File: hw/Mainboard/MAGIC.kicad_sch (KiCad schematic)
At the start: 18 parts, among them U7 SN74LVC4245APWR, U8 SN74LVC4245APWR, U9 SN74LVC4245APWR

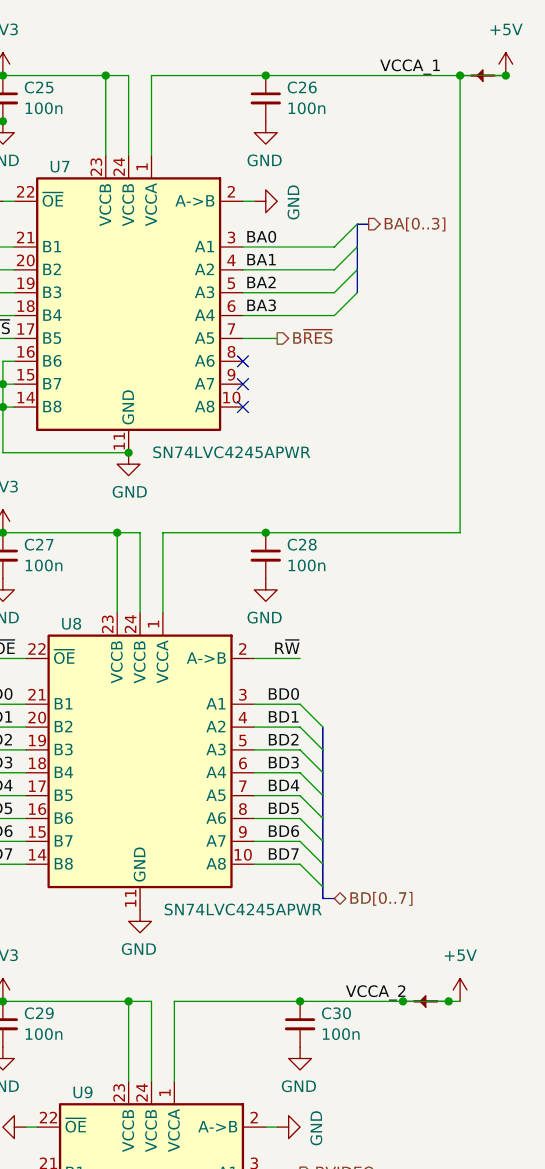
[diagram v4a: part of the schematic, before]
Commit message: hw: remove net/power ties
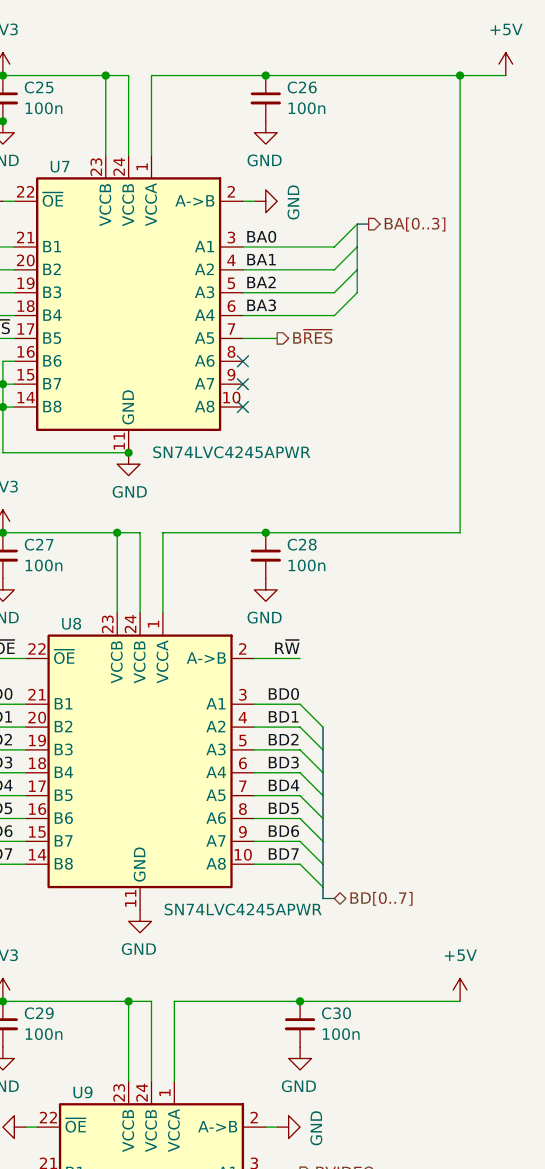
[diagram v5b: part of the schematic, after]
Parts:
- removed PT13, PT14: PowerTie_2, PET:NetTie-2_SMD_Pad_1.6_to_0.4mm, symbol PET:PowerTie_2
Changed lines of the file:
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@@
   (junction (at 207.01 57.15) (diameter 0) (color 0 0 0 0)
   )
-  (junction (at 262.89 20.32) (diameter 0) (color 0 0 0 0)
-  )
   (junction (at 220.98 62.23) (diameter 0) (color 0 0 0 0)
   )
   (junction (at 92.71 124.46) (diameter 0) (color 0 0 0 0)
   )
-  (junction (at 251.46 123.19) (diameter 0) (color 0 0 0 0)
-  )
   (junction (at 207.01 71.12) (diameter 0) (color 0 0 0 0)
   )
@@
   )
   (junction (at 96.52 116.84) (diameter 0) (color 0 0 0 0)
-  )
-  (junction (at 256.54 123.19) (diameter 0) (color 0 0 0 0)
   )
   (junction (at 219.71 71.12) (diameter 0) (color 0 0 0 0)
@@
     (stroke (width 0) (type default) (color 0 0 0 0))
   )
-  (wire (pts (xy 240.03 123.19) (xy 251.46 123.19))
+  (wire (pts (xy 240.03 123.19) (xy 257.81 123.19))
     (stroke (width 0) (type default) (color 0 0 0 0))
   )
@@
     (stroke (width 0) (type default) (color 0 0 0 0))
   )
-  (wire (pts (xy 251.46 123.19) (xy 256.54 123.19))
-    (stroke (width 0) (type default) (color 0 0 0 0))
-  )
   (wire (pts (xy 240.03 102.87) (xy 234.95 102.87))
     (stroke (width 0) (type default) (color 0 0 0 0))
@@
   )
   (bus (pts (xy 203.2 107.95) (xy 203.2 110.49))
-    (stroke (width 0) (type default) (color 0 0 0 0))
-  )
-  (wire (pts (xy 256.54 123.19) (xy 257.81 123.19))
     (stroke (width 0) (type default) (color 0 0 0 0))
   )
@@
     (effects (font (size 1.27 1.27)) (justify left bottom))
   )
-  (label "VCCA_1" (at 248.92 20.32 0)
-    (effects (font (size 1.27 1.27)) (justify left bottom))
-  )
   (label "A1" (at 201.93 41.91 0)
     (effects (font (size 1.27 1.27)) (justify left bottom))
@@
   )
   (label "D2" (at 205.74 95.25 0)
-    (effects (font (size 1.27 1.27)) (justify left bottom))
-  )
-  (label "VCCA_2" (at 245.11 123.19 0)
     (effects (font (size 1.27 1.27)) (justify left bottom))
   )
@@
     (pin "2")
   )
-  (symbol (lib_id "PET:PowerTie_2") (at 254 123.19 180) (unit 1)
-    (in_bom yes) (on_board yes) (fields_autoplaced)
-    (property "Reference" "PT14" (id 0) (at 254 125.095 0)
-      (effects (font (size 1.27 1.27)) hide)
-    )
-    (property "Value" "PowerTie_2" (id 1) (at 254 121.285 0)
-      (effects (font (size 1.27 1.27)) hide)
-    )
-    (property "Footprint" "PET:NetTie-2_SMD_Pad_1.6_to_0.4mm" (id 2) (at 254 123.19 0)
-      (effects (font (size 1.27 1.27)) hide)
-    )
-    (property "Datasheet" "~" (id 3) (at 254 123.19 0)
-      (effects (font (size 1.27 1.27)) hide)
-    )
-    (pin "1")
-    (pin "2")
-  )
   (symbol (lib_id "power:GND") (at 92.71 125.73 0) (unit 1)
     (in_bom yes) (on_board yes) (fields_autoplaced)
@@
     (pin "1")
   )
-  (symbol (lib_id "PET:PowerTie_2") (at 260.35 20.32 180) (unit 1)
-    (in_bom yes) (on_board yes) (fields_autoplaced)
-    (property "Reference" "PT13" (id 0) (at 260.35 22.225 0)
-      (effects (font (size 1.27 1.27)) hide)
-    )
-    (property "Value" "PowerTie_2" (id 1) (at 260.35 18.415 0)
-      (effects (font (size 1.27 1.27)) hide)
-    )
-    (property "Footprint" "PET:NetTie-2_SMD_Pad_1.6_to_0.4mm" (id 2) (at 260.35 20.32 0)
-      (effects (font (size 1.27 1.27)) hide)
-    )
-    (property "Datasheet" "~" (id 3) (at 260.35 20.32 0)
-      (effects (font (size 1.27 1.27)) hide)
-    )
-    (pin "1")
-    (pin "2")
-  )
   (symbol (lib_id "power:+3V3") (at 207.01 123.19 0) (mirror y) (unit 1)

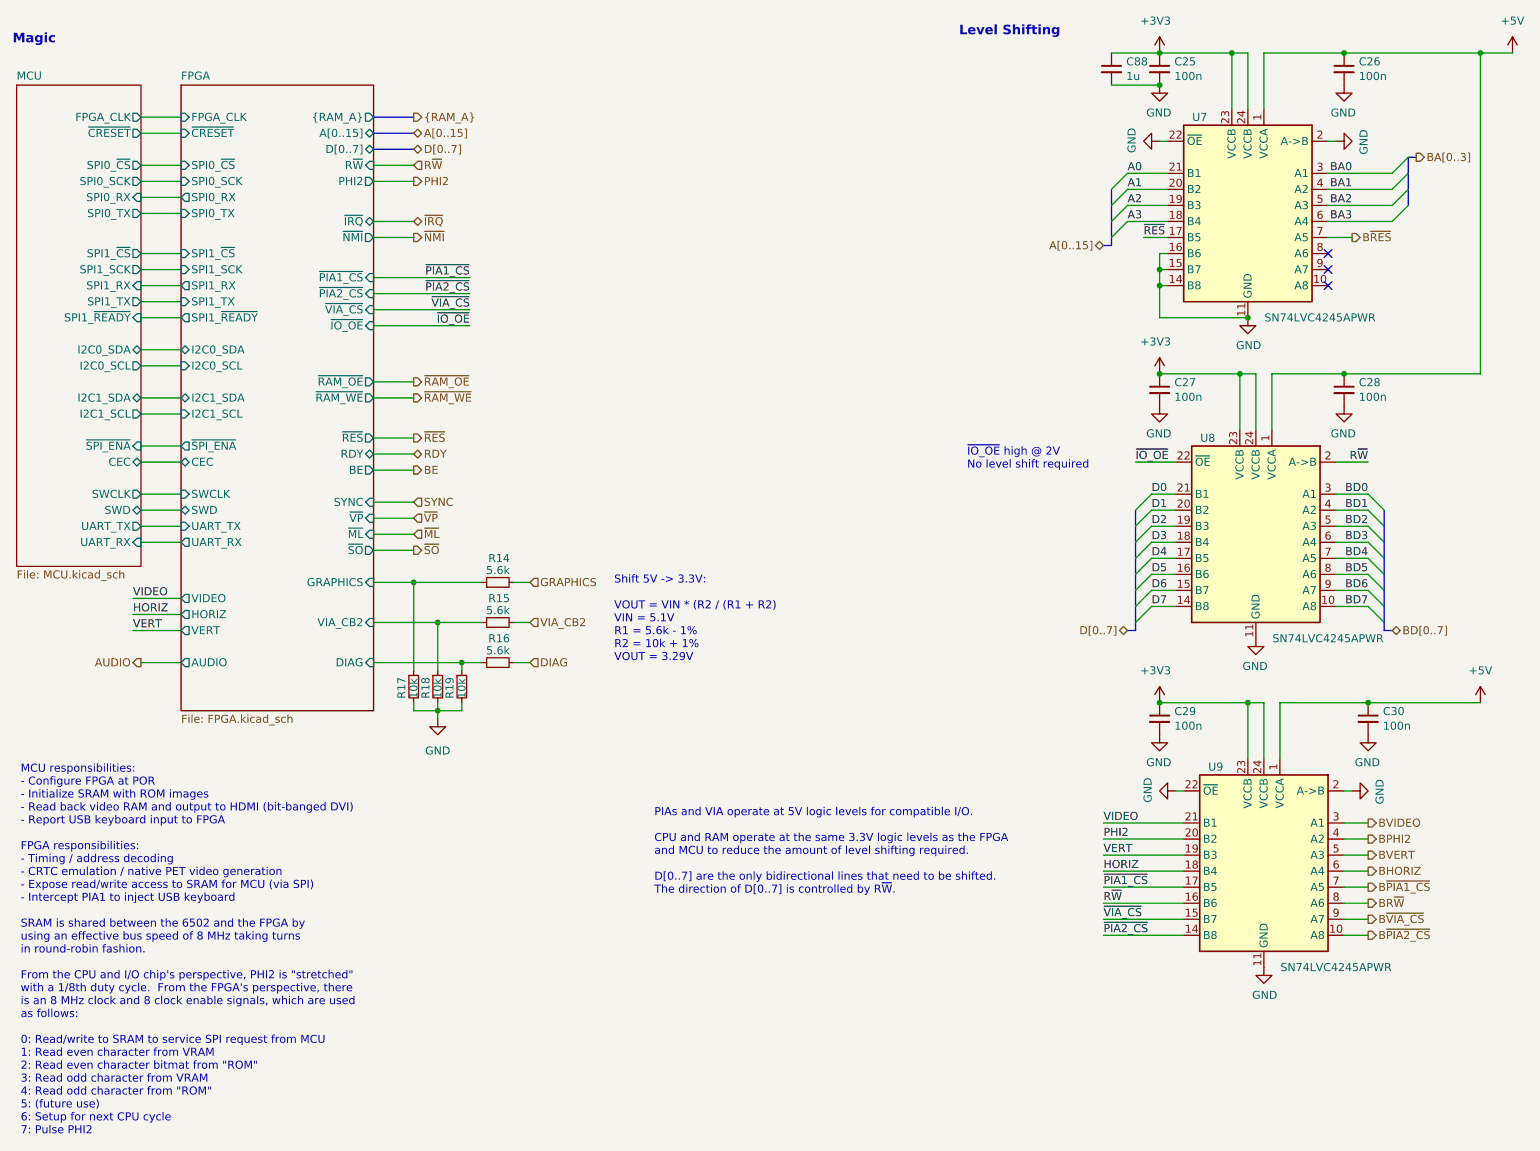
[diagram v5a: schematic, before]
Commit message: hw: renumber J* refs to match PET connectors
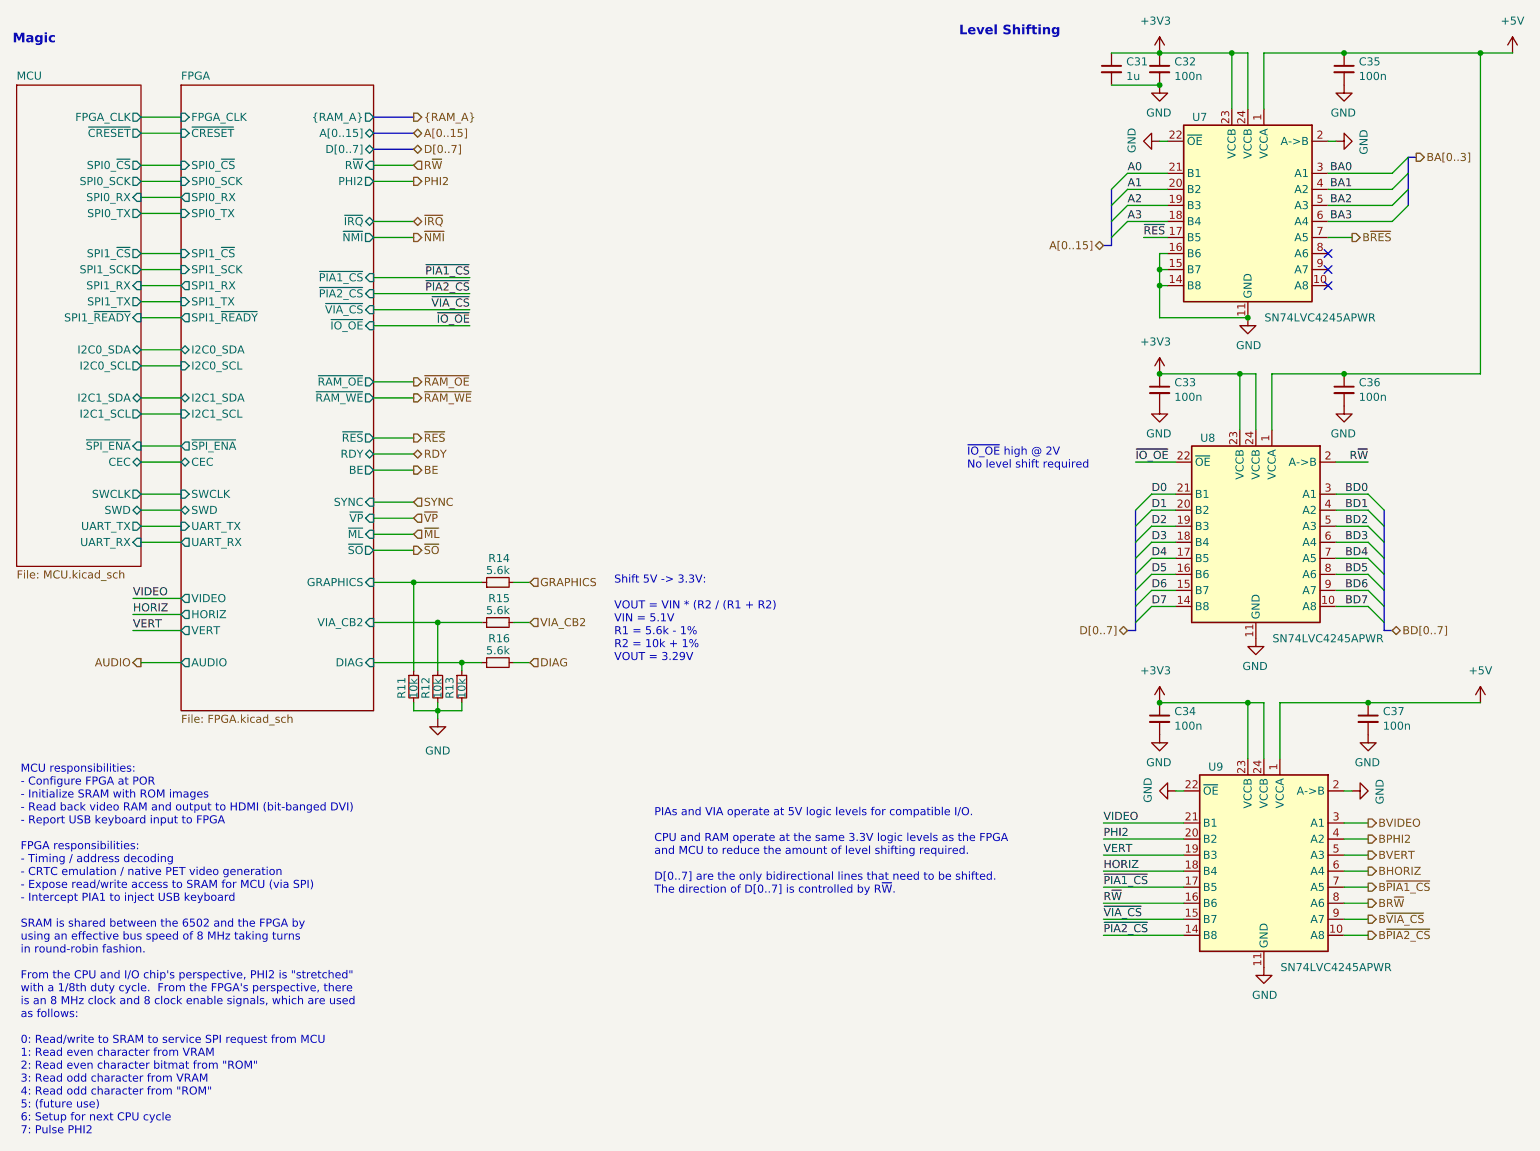
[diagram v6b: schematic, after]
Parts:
- renumbered C88 to C31, C25 to C32, C27 to C33, C29 to C34, C26 to C35, C28 to C36, C30 to C37, R17 to R11, R18 to R12, R19 to R13
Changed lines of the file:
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@@
   (symbol (lib_id "power:+3V3") (at 207.01 71.12 0) (mirror y) (unit 1)
     (in_bom yes) (on_board yes)
-    (property "Reference" "#PWR041" (id 0) (at 207.01 74.93 0)
+    (property "Reference" "#PWR037" (id 0) (at 207.01 74.93 0)
       (effects (font (size 1.27 1.27)) hide)
     )
@@
   (symbol (lib_id "power:GND") (at 220.98 62.23 0) (unit 1)
     (in_bom yes) (on_board yes)
-    (property "Reference" "#PWR040" (id 0) (at 220.98 68.58 0)
+    (property "Reference" "#PWR042" (id 0) (at 220.98 68.58 0)
       (effects (font (size 1.27 1.27)) hide)
     )
@@
   (symbol (lib_id "power:GND") (at 222.25 113.03 0) (mirror y) (unit 1)
     (in_bom yes) (on_board yes)
-    (property "Reference" "#PWR044" (id 0) (at 222.25 119.38 0)
+    (property "Reference" "#PWR043" (id 0) (at 222.25 119.38 0)
       (effects (font (size 1.27 1.27)) hide)
     )
@@
   (symbol (lib_id "power:GND") (at 223.52 165.1 0) (unit 1)
     (in_bom yes) (on_board yes)
-    (property "Reference" "#PWR052" (id 0) (at 223.52 171.45 0)
+    (property "Reference" "#PWR044" (id 0) (at 223.52 171.45 0)
       (effects (font (size 1.27 1.27)) hide)
     )
@@
   (symbol (lib_id "power:GND") (at 207.01 34.29 270) (mirror x) (unit 1)
     (in_bom yes) (on_board yes)
-    (property "Reference" "#PWR038" (id 0) (at 200.66 34.29 0)
+    (property "Reference" "#PWR036" (id 0) (at 200.66 34.29 0)
       (effects (font (size 1.27 1.27)) hide)
     )
@@
   (symbol (lib_id "Device:C_Small") (at 207.01 22.86 0) (unit 1)
     (in_bom yes) (on_board yes)
-    (property "Reference" "C25" (id 0) (at 209.3468 21.6916 0)
+    (property "Reference" "C32" (id 0) (at 209.3468 21.6916 0)
       (effects (font (size 1.27 1.27)) (justify left))
     )
@@
   (symbol (lib_id "Device:C_Small") (at 207.01 125.73 0) (unit 1)
     (in_bom yes) (on_board yes)
-    (property "Reference" "C29" (id 0) (at 209.3468 124.5616 0)
+    (property "Reference" "C34" (id 0) (at 209.3468 124.5616 0)
       (effects (font (size 1.27 1.27)) (justify left))
     )
@@
   (symbol (lib_id "power:GND") (at 209.55 137.16 270) (mirror x) (unit 1)
     (in_bom yes) (on_board yes)
-    (property "Reference" "#PWR050" (id 0) (at 203.2 137.16 0)
+    (property "Reference" "#PWR041" (id 0) (at 203.2 137.16 0)
       (effects (font (size 1.27 1.27)) hide)
     )
@@
   (symbol (lib_id "power:GND") (at 237.49 137.16 90) (mirror x) (unit 1)
     (in_bom yes) (on_board yes)
-    (property "Reference" "#PWR051" (id 0) (at 243.84 137.16 0)
+    (property "Reference" "#PWR048" (id 0) (at 243.84 137.16 0)
       (effects (font (size 1.27 1.27)) hide)
     )
@@
   (symbol (lib_id "power:GND") (at 234.95 34.29 90) (mirror x) (unit 1)
     (in_bom yes) (on_board yes)
-    (property "Reference" "#PWR039" (id 0) (at 241.3 34.29 0)
+    (property "Reference" "#PWR045" (id 0) (at 241.3 34.29 0)
       (effects (font (size 1.27 1.27)) hide)
     )
@@
   (symbol (lib_id "Device:C_Small") (at 236.22 22.86 0) (unit 1)
     (in_bom yes) (on_board yes)
-    (property "Reference" "C26" (id 0) (at 238.5568 21.6916 0)
+    (property "Reference" "C35" (id 0) (at 238.5568 21.6916 0)
       (effects (font (size 1.27 1.27)) (justify left))
     )
@@
   (symbol (lib_id "Device:C_Small") (at 240.03 125.73 0) (unit 1)
     (in_bom yes) (on_board yes)
-    (property "Reference" "C30" (id 0) (at 242.3668 124.5616 0)
+    (property "Reference" "C37" (id 0) (at 242.3668 124.5616 0)
       (effects (font (size 1.27 1.27)) (justify left))
     )
@@
   (symbol (lib_id "Device:C_Small") (at 236.22 73.66 0) (unit 1)
     (in_bom yes) (on_board yes)
-    (property "Reference" "C28" (id 0) (at 238.5568 72.4916 0)
+    (property "Reference" "C36" (id 0) (at 238.5568 72.4916 0)
       (effects (font (size 1.27 1.27)) (justify left))
     )
@@
   (symbol (lib_id "Device:C_Small") (at 207.01 73.66 0) (unit 1)
     (in_bom yes) (on_board yes)
-    (property "Reference" "C27" (id 0) (at 209.3468 72.4916 0)
+    (property "Reference" "C33" (id 0) (at 209.3468 72.4916 0)
       (effects (font (size 1.27 1.27)) (justify left))
     )
@@
   (symbol (lib_id "Device:C_Small") (at 199.39 22.86 0) (unit 1)
     (in_bom yes) (on_board yes)
-    (property "Reference" "C88" (id 0) (at 201.7268 21.6916 0)
+    (property "Reference" "C31" (id 0) (at 201.7268 21.6916 0)
       (effects (font (size 1.27 1.27)) (justify left))
     )
@@
   (symbol (lib_id "power:GND") (at 207.01 25.4 0) (mirror y) (unit 1)
     (in_bom yes) (on_board yes)
-    (property "Reference" "#PWR036" (id 0) (at 207.01 31.75 0)
+    (property "Reference" "#PWR035" (id 0) (at 207.01 31.75 0)
       (effects (font (size 1.27 1.27)) hide)
     )
@@
   (symbol (lib_id "power:+5V") (at 257.81 123.19 0) (unit 1)
     (in_bom yes) (on_board yes) (fields_autoplaced)
-    (property "Reference" "#PWR046" (id 0) (at 257.81 127 0)
+    (property "Reference" "#PWR050" (id 0) (at 257.81 127 0)
       (effects (font (size 1.27 1.27)) hide)
     )
@@
   (symbol (lib_id "power:GND") (at 92.71 125.73 0) (unit 1)
     (in_bom yes) (on_board yes) (fields_autoplaced)
-    (property "Reference" "#PWR047" (id 0) (at 92.71 132.08 0)
+    (property "Reference" "#PWR033" (id 0) (at 92.71 132.08 0)
       (effects (font (size 1.27 1.27)) hide)
     )
@@
   (symbol (lib_id "power:GND") (at 236.22 76.2 0) (mirror y) (unit 1)
     (in_bom yes) (on_board yes)
-    (property "Reference" "#PWR043" (id 0) (at 236.22 82.55 0)
+    (property "Reference" "#PWR047" (id 0) (at 236.22 82.55 0)
       (effects (font (size 1.27 1.27)) hide)
     )
@@
   (symbol (lib_id "Device:R_Small") (at 96.52 120.65 0) (unit 1)
     (in_bom yes) (on_board yes)
-    (property "Reference" "R19" (id 0) (at 94.615 122.555 90)
+    (property "Reference" "R13" (id 0) (at 94.615 122.555 90)
       (effects (font (size 1.27 1.27)) (justify left))
     )
@@
   (symbol (lib_id "power:+5V") (at 262.89 20.32 0) (unit 1)
     (in_bom yes) (on_board yes) (fields_autoplaced)
-    (property "Reference" "#PWR035" (id 0) (at 262.89 24.13 0)
+    (property "Reference" "#PWR051" (id 0) (at 262.89 24.13 0)
       (effects (font (size 1.27 1.27)) hide)
     )
@@
   (symbol (lib_id "power:GND") (at 236.22 25.4 0) (mirror y) (unit 1)
     (in_bom yes) (on_board yes)
-    (property "Reference" "#PWR037" (id 0) (at 236.22 31.75 0)
+    (property "Reference" "#PWR046" (id 0) (at 236.22 31.75 0)
       (effects (font (size 1.27 1.27)) hide)
     )
@@
   (symbol (lib_id "power:+3V3") (at 207.01 123.19 0) (mirror y) (unit 1)
     (in_bom yes) (on_board yes)
-    (property "Reference" "#PWR045" (id 0) (at 207.01 127 0)
+    (property "Reference" "#PWR039" (id 0) (at 207.01 127 0)
       (effects (font (size 1.27 1.27)) hide)
     )
@@
   (symbol (lib_id "power:GND") (at 207.01 128.27 0) (mirror y) (unit 1)
     (in_bom yes) (on_board yes)
-    (property "Reference" "#PWR048" (id 0) (at 207.01 134.62 0)
+    (property "Reference" "#PWR040" (id 0) (at 207.01 134.62 0)
       (effects (font (size 1.27 1.27)) hide)
     )
@@
   (symbol (lib_id "Device:R_Small") (at 88.9 120.65 0) (unit 1)
     (in_bom yes) (on_board yes)
-    (property "Reference" "R17" (id 0) (at 86.995 122.555 90)
+    (property "Reference" "R11" (id 0) (at 86.995 122.555 90)
       (effects (font (size 1.27 1.27)) (justify left))
     )
@@
   (symbol (lib_id "power:GND") (at 207.01 76.2 0) (mirror y) (unit 1)
     (in_bom yes) (on_board yes)
-    (property "Reference" "#PWR042" (id 0) (at 207.01 82.55 0)
+    (property "Reference" "#PWR038" (id 0) (at 207.01 82.55 0)
       (effects (font (size 1.27 1.27)) hide)
     )
@@
   (symbol (lib_id "Device:R_Small") (at 92.71 120.65 0) (unit 1)
     (in_bom yes) (on_board yes)
-    (property "Reference" "R18" (id 0) (at 90.805 122.555 90)
-      (effects (font (size 1.27 1.27)) (justify left))
-    )
+    (property "Reference" "R12" (id 0) (at 90.805 122.555 90)
+      (effects (font (size 1.27 1.27)) (justify left))
+    )
